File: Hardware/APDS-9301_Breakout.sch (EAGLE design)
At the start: 14 parts, among them U1 APDS-9301

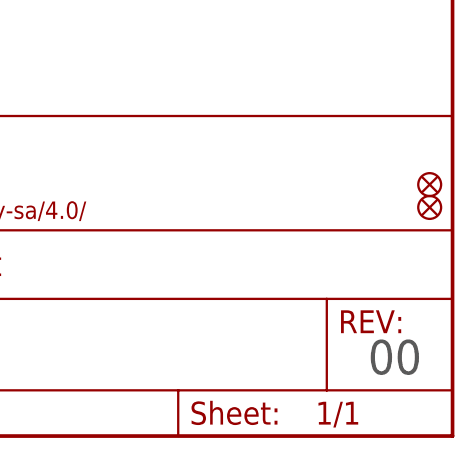
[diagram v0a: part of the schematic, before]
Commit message: Change to V10, chg silk on back of board
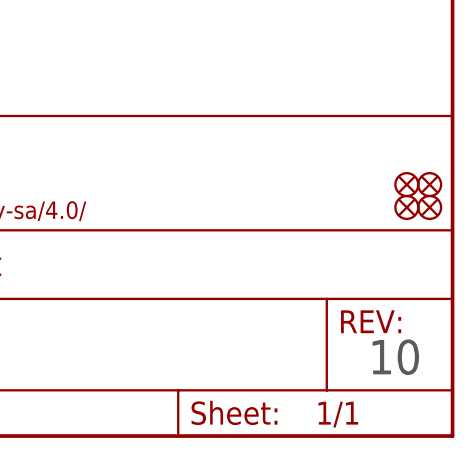
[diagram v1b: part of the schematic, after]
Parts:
- added FD3, FD4: FIDUCIALUFIDUCIAL, SparkFun-Aesthetics:FIDUCIALUFIDUCIAL
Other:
- note added: "10"
- note removed: "00"
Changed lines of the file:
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@@
 <?xml version="1.0" encoding="utf-8"?>
 <!DOCTYPE eagle SYSTEM "eagle.dtd">
-<eagle version="7.7.0">
+<eagle version="7.6.0">
 <drawing>
 <settings>
@@
 <part name="FD1" library="SparkFun-Aesthetics" deviceset="FIDUCIAL" device="UFIDUCIAL"/>
 <part name="FD2" library="SparkFun-Aesthetics" deviceset="FIDUCIAL" device="UFIDUCIAL"/>
+<part name="FD3" library="SparkFun-Aesthetics" deviceset="FIDUCIAL" device="UFIDUCIAL"/>
+<part name="FD4" library="SparkFun-Aesthetics" deviceset="FIDUCIAL" device="UFIDUCIAL"/>
 </parts>
 <sheets>
@@
 0x49 - LOW</text>
 <text x="165.1" y="7.62" size="3.81" layer="97">M. Hord</text>
-<text x="239.522" y="6.858" size="3.81" layer="97">00</text>
+<text x="239.522" y="6.858" size="3.81" layer="97">10</text>
 </plain>
 <instances>
@@
 <instance part="FD1" gate="G$1" x="246.38" y="25.4"/>
 <instance part="FD2" gate="G$1" x="246.38" y="27.94"/>
+<instance part="FD3" gate="G$1" x="243.84" y="27.94"/>
+<instance part="FD4" gate="G$1" x="243.84" y="25.4"/>
 </instances>
 <busses>

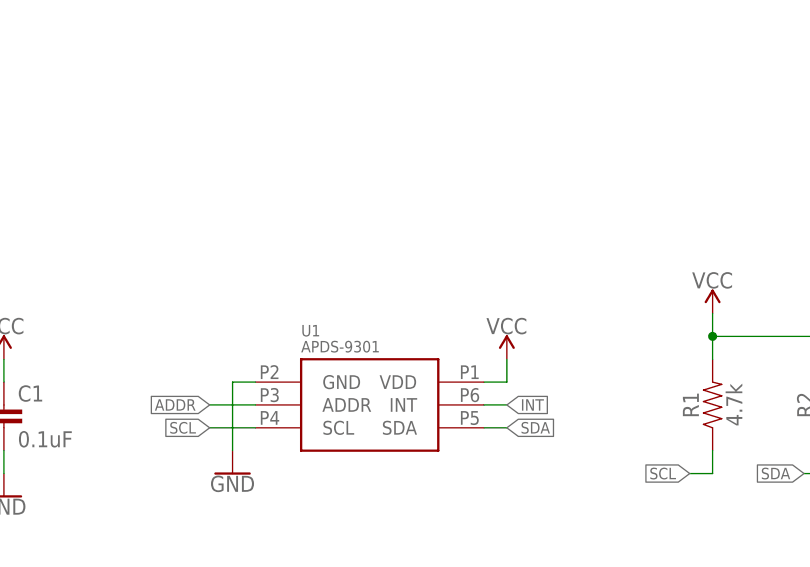
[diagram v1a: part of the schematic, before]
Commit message: Changes for V10 post checklist
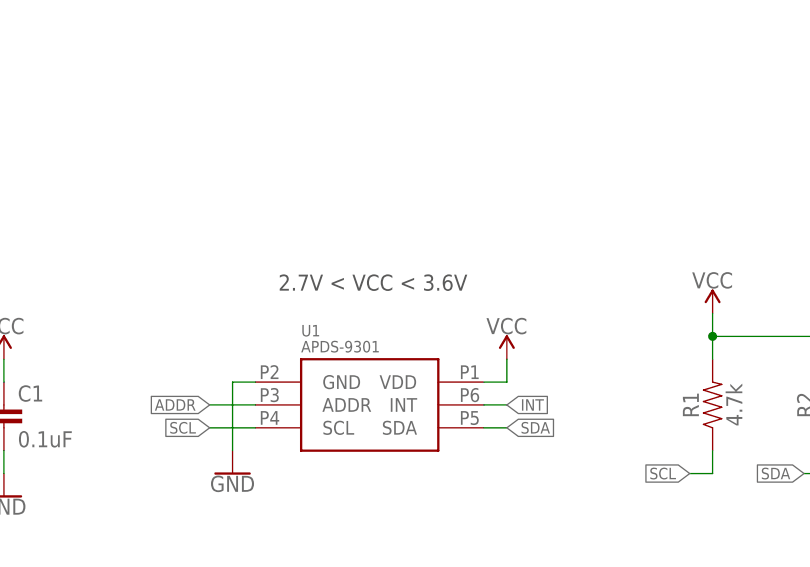
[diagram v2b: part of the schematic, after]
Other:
- note added: "2.7V < VCC < 3.6V"
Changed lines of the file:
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@@
 <?xml version="1.0" encoding="utf-8"?>
 <!DOCTYPE eagle SYSTEM "eagle.dtd">
-<eagle version="7.6.0">
+<eagle version="7.7.0">
 <drawing>
 <settings>
@@
 <text x="165.1" y="7.62" size="3.81" layer="97">M. Hord</text>
 <text x="239.522" y="6.858" size="3.81" layer="97">10</text>
+<text x="129.54" y="116.84" size="1.778" layer="97">2.7V &lt; VCC &lt; 3.6V</text>
 </plain>
 <instances>
